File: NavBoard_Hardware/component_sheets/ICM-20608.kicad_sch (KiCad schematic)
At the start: 9 parts

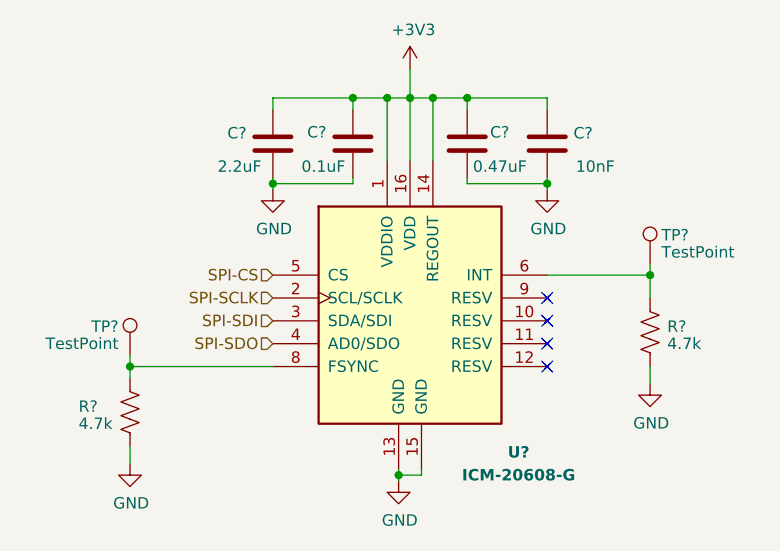
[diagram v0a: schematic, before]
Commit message: Created adapter symbols and footprints
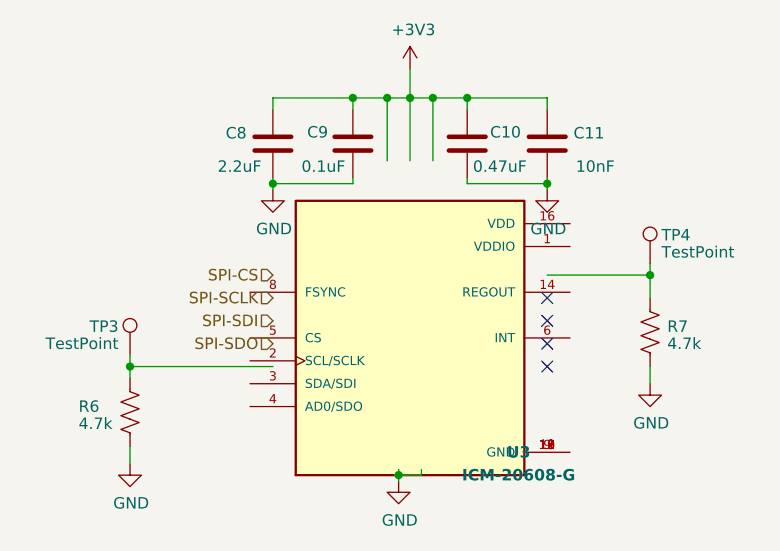
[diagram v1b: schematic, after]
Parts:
- gave numbers to parts that had none: 9
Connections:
- net +3V3: no longer U3.1 (VDDIO), U3.14 (REGOUT), U3.16 (VDD)
- net GND: no longer U3.13 (GND), U3.15 (GND)
- net SPI-CS: no longer U3.5 (CS)
- net SPI-SCLK: no longer U3.2 (SCL/SCLK)
- net SPI-SDI: no longer U3.3 (SDA/SDI)
- net SPI-SDO: no longer U3.4 (AD0/SDO)
- net at R6.1, TP3.1: no longer U3.8 (FSYNC)
- net at R7.1, TP4.1: no longer U3.6 (INT)
- net at U3.10 (GND): now also U3.11 (GND), U3.12 (GND), U3.13 (GND), U3.15 (GND), U3.9 (GND)
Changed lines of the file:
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@@
   (symbol (lib_id "Device:R_US") (at 117.475 106.045 0) (unit 1)
     (in_bom yes) (on_board yes)
-    (property "Reference" "R?" (id 0) (at 111.76 105.41 0)
+    (property "Reference" "R6" (id 0) (at 111.76 105.41 0)
       (effects (font (size 1.27 1.27)) (justify left))
     )
@@
   (symbol (lib_id "Device:R_US") (at 175.26 97.155 0) (unit 1)
     (in_bom yes) (on_board yes)
-    (property "Reference" "R?" (id 0) (at 177.165 96.52 0)
+    (property "Reference" "R7" (id 0) (at 177.165 96.52 0)
       (effects (font (size 1.27 1.27)) (justify left))
     )
@@
   (symbol (lib_id "Device:C") (at 142.24 76.2 0) (unit 1)
     (in_bom yes) (on_board yes)
-    (property "Reference" "C?" (id 0) (at 137.16 74.93 0)
+    (property "Reference" "C9" (id 0) (at 137.16 74.93 0)
       (effects (font (size 1.27 1.27)) (justify left))
     )
@@
   (symbol (lib_id "power:GND") (at 163.83 81.28 0) (unit 1)
     (in_bom yes) (on_board yes)
-    (property "Reference" "#PWR?" (id 0) (at 163.83 87.63 0)
+    (property "Reference" "#PWR014" (id 0) (at 163.83 87.63 0)
       (effects (font (size 1.27 1.27)) hide)
     )
@@
   (symbol (lib_id "Device:C") (at 133.35 76.2 0) (mirror y) (unit 1)
     (in_bom yes) (on_board yes)
-    (property "Reference" "C?" (id 0) (at 130.429 75.0316 0)
+    (property "Reference" "C8" (id 0) (at 130.429 75.0316 0)
       (effects (font (size 1.27 1.27)) (justify left))
     )
@@
   (symbol (lib_id "power:GND") (at 175.26 102.87 0) (unit 1)
     (in_bom yes) (on_board yes)
-    (property "Reference" "#PWR?" (id 0) (at 175.26 109.22 0)
+    (property "Reference" "#PWR015" (id 0) (at 175.26 109.22 0)
       (effects (font (size 1.27 1.27)) hide)
     )
@@
   (symbol (lib_id "Device:C") (at 163.83 76.2 0) (unit 1)
     (in_bom yes) (on_board yes)
-    (property "Reference" "C?" (id 0) (at 166.751 75.0316 0)
+    (property "Reference" "C11" (id 0) (at 166.751 75.0316 0)
       (effects (font (size 1.27 1.27)) (justify left))
     )
@@
   (symbol (lib_id "power:GND") (at 133.35 81.28 0) (unit 1)
     (in_bom yes) (on_board yes)
-    (property "Reference" "#PWR?" (id 0) (at 133.35 87.63 0)
+    (property "Reference" "#PWR011" (id 0) (at 133.35 87.63 0)
       (effects (font (size 1.27 1.27)) hide)
     )
@@
   (symbol (lib_id "power:GND") (at 117.475 111.76 0) (unit 1)
     (in_bom yes) (on_board yes)
-    (property "Reference" "#PWR?" (id 0) (at 117.475 118.11 0)
+    (property "Reference" "#PWR010" (id 0) (at 117.475 118.11 0)
       (effects (font (size 1.27 1.27)) hide)
     )
@@
   (symbol (lib_id "Connector:TestPoint") (at 117.475 99.695 0) (mirror y) (unit 1)
     (in_bom yes) (on_board yes)
-    (property "Reference" "TP?" (id 0) (at 116.205 96.52 0)
+    (property "Reference" "TP3" (id 0) (at 116.205 96.52 0)
       (effects (font (size 1.27 1.27)) (justify left))
     )
@@
   (symbol (lib_id "power:GND") (at 147.32 113.665 0) (unit 1)
     (in_bom yes) (on_board yes)
-    (property "Reference" "#PWR?" (id 0) (at 147.32 120.015 0)
+    (property "Reference" "#PWR012" (id 0) (at 147.32 120.015 0)
       (effects (font (size 1.27 1.27)) hide)
     )
@@
   (symbol (lib_id "Device:C") (at 154.94 76.2 0) (unit 1)
     (in_bom yes) (on_board yes)
-    (property "Reference" "C?" (id 0) (at 157.48 74.93 0)
+    (property "Reference" "C10" (id 0) (at 157.48 74.93 0)
       (effects (font (size 1.27 1.27)) (justify left))
     )
@@
   (symbol (lib_id "MRDT_Sensors:ICM-20608-G") (at 148.59 97.79 0) (unit 1)
     (in_bom yes) (on_board yes)
-    (property "Reference" "U?" (id 0) (at 160.655 110.49 0)
+    (property "Reference" "U3" (id 0) (at 160.655 110.49 0)
       (effects (font (size 1.27 1.27) bold))
     )
@@
   (symbol (lib_id "power:+3V3") (at 148.59 67.945 0) (unit 1)
     (in_bom yes) (on_board yes)
-    (property "Reference" "#PWR?" (id 0) (at 148.59 71.755 0)
+    (property "Reference" "#PWR013" (id 0) (at 148.59 71.755 0)
       (effects (font (size 1.27 1.27)) hide)
     )
@@
   (symbol (lib_id "Connector:TestPoint") (at 175.26 89.535 0) (unit 1)
     (in_bom yes) (on_board yes)
-    (property "Reference" "TP?" (id 0) (at 176.53 86.36 0)
-      (effects (font (size 1.27 1.27)) (justify left))
-    )
+    (property "Reference" "TP4" (id 0) (at 176.53 86.36 0)
+      (effects (font (size 1.27 1.27)) (justify left))
+    )

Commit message: Updated BMI component sheet from Navboard_2023_rev2
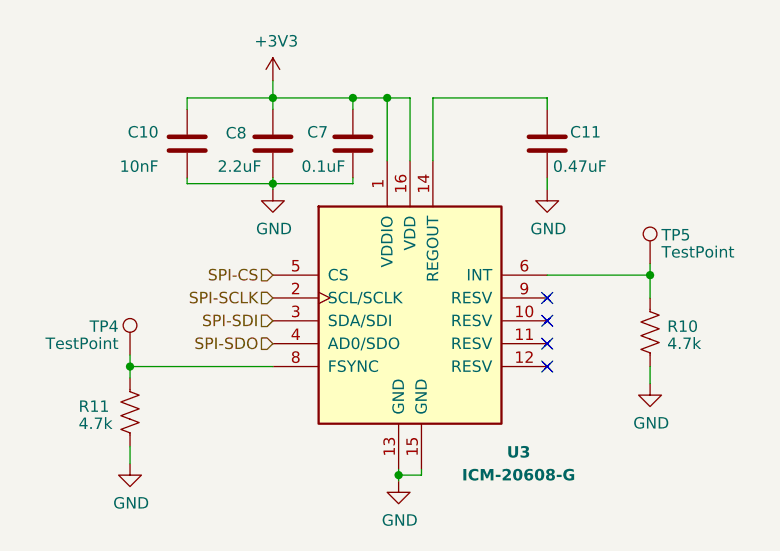
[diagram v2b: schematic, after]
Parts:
- renumbered C11 to C10, C10 to C11, C9 to C7, R7 to R10, R6 to R11, TP3 to TP4, TP4 to TP5
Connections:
- net +3V3: now also U3.1 (VDDIO), U3.16 (VDD); no longer C11.1
- net GND: now also U3.13 (GND), U3.15 (GND)
- net SPI-CS: now also U3.5 (CS)
- net SPI-SCLK: now also U3.2 (SCL/SCLK)
- net SPI-SDI: now also U3.3 (SDA/SDI)
- net SPI-SDO: now also U3.4 (AD0/SDO)
- net at R11.1, TP4.1: now also U3.8 (FSYNC)
- net at R10.1, TP5.1: now also U3.6 (INT)
- net at U3.14 (REGOUT): now also C11.1
- now unconnected: U3.10 (GND), U3.11 (GND), U3.12 (GND), U3.9 (GND)
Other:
- company: Missouri S&T Rover Design Team -> Thomas Francois, Katherine Dunlap, Missouri S&T Mars Rover Design Team
- moved on the sheet: C10, C11

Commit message: Most schematic connections completed
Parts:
- U3: footprint ICM-20608-G:ICM-20608-G -> PQFN50P300X300X80-16N
- renumbered C11 to C10, C10 to C11, C7 to C9, R11 to R6, R10 to R7, TP4 to TP3, TP5 to TP4
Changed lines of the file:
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@@
   (symbol (lib_id "Device:R_US") (at 117.475 106.045 0) (unit 1)
     (in_bom yes) (on_board yes)
-    (property "Reference" "R11" (id 0) (at 111.76 105.41 0)
+    (property "Reference" "R6" (id 0) (at 111.76 105.41 0)
       (effects (font (size 1.27 1.27)) (justify left))
     )
@@
   (symbol (lib_id "Device:R_US") (at 175.26 97.155 0) (unit 1)
     (in_bom yes) (on_board yes)
-    (property "Reference" "R10" (id 0) (at 177.165 96.52 0)
+    (property "Reference" "R7" (id 0) (at 177.165 96.52 0)
       (effects (font (size 1.27 1.27)) (justify left))
     )
@@
   (symbol (lib_id "Device:C") (at 142.24 76.2 0) (unit 1)
     (in_bom yes) (on_board yes)
-    (property "Reference" "C7" (id 0) (at 137.16 74.93 0)
+    (property "Reference" "C9" (id 0) (at 137.16 74.93 0)
       (effects (font (size 1.27 1.27)) (justify left))
     )
@@
   (symbol (lib_id "power:GND") (at 163.83 81.28 0) (unit 1)
     (in_bom yes) (on_board yes)
-    (property "Reference" "#PWR0104" (id 0) (at 163.83 87.63 0)
+    (property "Reference" "#PWR014" (id 0) (at 163.83 87.63 0)
       (effects (font (size 1.27 1.27)) hide)
     )
@@
   (symbol (lib_id "power:GND") (at 175.26 102.87 0) (unit 1)
     (in_bom yes) (on_board yes)
-    (property "Reference" "#PWR0101" (id 0) (at 175.26 109.22 0)
+    (property "Reference" "#PWR015" (id 0) (at 175.26 109.22 0)
       (effects (font (size 1.27 1.27)) hide)
     )
@@
   (symbol (lib_id "Device:C") (at 123.825 76.2 0) (mirror y) (unit 1)
     (in_bom yes) (on_board yes)
-    (property "Reference" "C10" (id 0) (at 120.65 74.93 0)
+    (property "Reference" "C11" (id 0) (at 120.65 74.93 0)
       (effects (font (size 1.27 1.27)) (justify left))
     )
@@
   (symbol (lib_id "power:GND") (at 133.35 81.28 0) (unit 1)
     (in_bom yes) (on_board yes)
-    (property "Reference" "#PWR0106" (id 0) (at 133.35 87.63 0)
+    (property "Reference" "#PWR011" (id 0) (at 133.35 87.63 0)
       (effects (font (size 1.27 1.27)) hide)
     )
@@
   (symbol (lib_id "power:GND") (at 117.475 111.76 0) (unit 1)
     (in_bom yes) (on_board yes)
-    (property "Reference" "#PWR0107" (id 0) (at 117.475 118.11 0)
+    (property "Reference" "#PWR010" (id 0) (at 117.475 118.11 0)
       (effects (font (size 1.27 1.27)) hide)
     )
@@
   (symbol (lib_id "Connector:TestPoint") (at 117.475 99.695 0) (mirror y) (unit 1)
     (in_bom yes) (on_board yes)
-    (property "Reference" "TP4" (id 0) (at 116.205 96.52 0)
+    (property "Reference" "TP3" (id 0) (at 116.205 96.52 0)
       (effects (font (size 1.27 1.27)) (justify left))
     )
@@
   (symbol (lib_id "power:GND") (at 147.32 113.665 0) (unit 1)
     (in_bom yes) (on_board yes)
-    (property "Reference" "#PWR0105" (id 0) (at 147.32 120.015 0)
+    (property "Reference" "#PWR012" (id 0) (at 147.32 120.015 0)
       (effects (font (size 1.27 1.27)) hide)
     )
@@
   (symbol (lib_id "Device:C") (at 163.83 76.2 0) (unit 1)
     (in_bom yes) (on_board yes)
-    (property "Reference" "C11" (id 0) (at 166.37 74.93 0)
+    (property "Reference" "C10" (id 0) (at 166.37 74.93 0)
       (effects (font (size 1.27 1.27)) (justify left))
     )
@@
       (effects (font (size 1.27 1.27) bold))
     )
-    (property "Footprint" "ICM-20608-G:ICM-20608-G" (id 2) (at 173.99 85.725 0)
+    (property "Footprint" "PQFN50P300X300X80-16N" (id 2) (at 173.99 85.725 0)
       (effects (font (size 1.27 1.27)) (justify left bottom) hide)
     )
@@
   (symbol (lib_id "power:+3V3") (at 133.35 69.215 0) (unit 1)
     (in_bom yes) (on_board yes)
-    (property "Reference" "#PWR0103" (id 0) (at 133.35 73.025 0)
+    (property "Reference" "#PWR013" (id 0) (at 133.35 73.025 0)
       (effects (font (size 1.27 1.27)) hide)
     )
@@
   (symbol (lib_id "Connector:TestPoint") (at 175.26 89.535 0) (unit 1)
     (in_bom yes) (on_board yes)
-    (property "Reference" "TP5" (id 0) (at 176.53 86.36 0)
-      (effects (font (size 1.27 1.27)) (justify left))
-    )
+    (property "Reference" "TP4" (id 0) (at 176.53 86.36 0)
+      (effects (font (size 1.27 1.27)) (justify left))
+    )

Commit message: Annotated Schematic, assigned footprints, recovered accelerometer footprints
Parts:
- U3: footprint PQFN50P300X300X80-16N -> Nav_Board:ICM-20608-G
- renumbered C9 to C10, C10 to C11, C11 to C8, C8 to C9, R7 to R6, R6 to R7, TP4 to TP3, TP3 to TP4
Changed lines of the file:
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@@
   (symbol (lib_id "Device:R_US") (at 117.475 106.045 0) (unit 1)
     (in_bom yes) (on_board yes)
-    (property "Reference" "R6" (id 0) (at 111.76 105.41 0)
+    (property "Reference" "R7" (id 0) (at 111.76 105.41 0)
       (effects (font (size 1.27 1.27)) (justify left))
     )
@@
   (symbol (lib_id "Device:R_US") (at 175.26 97.155 0) (unit 1)
     (in_bom yes) (on_board yes)
-    (property "Reference" "R7" (id 0) (at 177.165 96.52 0)
+    (property "Reference" "R6" (id 0) (at 177.165 96.52 0)
       (effects (font (size 1.27 1.27)) (justify left))
     )
@@
   (symbol (lib_id "Device:C") (at 142.24 76.2 0) (unit 1)
     (in_bom yes) (on_board yes)
-    (property "Reference" "C9" (id 0) (at 137.16 74.93 0)
+    (property "Reference" "C10" (id 0) (at 137.16 74.93 0)
       (effects (font (size 1.27 1.27)) (justify left))
     )
@@
   (symbol (lib_id "power:GND") (at 163.83 81.28 0) (unit 1)
     (in_bom yes) (on_board yes)
-    (property "Reference" "#PWR014" (id 0) (at 163.83 87.63 0)
+    (property "Reference" "#PWR015" (id 0) (at 163.83 87.63 0)
       (effects (font (size 1.27 1.27)) hide)
     )
@@
   (symbol (lib_id "Device:C") (at 133.35 76.2 0) (mirror y) (unit 1)
     (in_bom yes) (on_board yes)
-    (property "Reference" "C8" (id 0) (at 130.429 75.0316 0)
+    (property "Reference" "C9" (id 0) (at 130.429 75.0316 0)
       (effects (font (size 1.27 1.27)) (justify left))
     )
@@
   (symbol (lib_id "power:GND") (at 175.26 102.87 0) (unit 1)
     (in_bom yes) (on_board yes)
-    (property "Reference" "#PWR015" (id 0) (at 175.26 109.22 0)
+    (property "Reference" "#PWR016" (id 0) (at 175.26 109.22 0)
       (effects (font (size 1.27 1.27)) hide)
     )
@@
   (symbol (lib_id "Device:C") (at 123.825 76.2 0) (mirror y) (unit 1)
     (in_bom yes) (on_board yes)
-    (property "Reference" "C11" (id 0) (at 120.65 74.93 0)
+    (property "Reference" "C8" (id 0) (at 120.65 74.93 0)
       (effects (font (size 1.27 1.27)) (justify left))
     )
@@
   (symbol (lib_id "power:GND") (at 133.35 81.28 0) (unit 1)
     (in_bom yes) (on_board yes)
-    (property "Reference" "#PWR011" (id 0) (at 133.35 87.63 0)
+    (property "Reference" "#PWR014" (id 0) (at 133.35 87.63 0)
       (effects (font (size 1.27 1.27)) hide)
     )
@@
   (symbol (lib_id "power:GND") (at 117.475 111.76 0) (unit 1)
     (in_bom yes) (on_board yes)
-    (property "Reference" "#PWR010" (id 0) (at 117.475 118.11 0)
+    (property "Reference" "#PWR017" (id 0) (at 117.475 118.11 0)
       (effects (font (size 1.27 1.27)) hide)
     )
@@
   (symbol (lib_id "Connector:TestPoint") (at 117.475 99.695 0) (mirror y) (unit 1)
     (in_bom yes) (on_board yes)
-    (property "Reference" "TP3" (id 0) (at 116.205 96.52 0)
+    (property "Reference" "TP4" (id 0) (at 116.205 96.52 0)
       (effects (font (size 1.27 1.27)) (justify left))
     )
@@
   (symbol (lib_id "power:GND") (at 147.32 113.665 0) (unit 1)
     (in_bom yes) (on_board yes)
-    (property "Reference" "#PWR012" (id 0) (at 147.32 120.015 0)
+    (property "Reference" "#PWR018" (id 0) (at 147.32 120.015 0)
       (effects (font (size 1.27 1.27)) hide)
     )
@@
   (symbol (lib_id "Device:C") (at 163.83 76.2 0) (unit 1)
     (in_bom yes) (on_board yes)
-    (property "Reference" "C10" (id 0) (at 166.37 74.93 0)
+    (property "Reference" "C11" (id 0) (at 166.37 74.93 0)
       (effects (font (size 1.27 1.27)) (justify left))
     )
@@
       (effects (font (size 1.27 1.27) bold))
     )
-    (property "Footprint" "PQFN50P300X300X80-16N" (id 2) (at 173.99 85.725 0)
+    (property "Footprint" "Nav_Board:ICM-20608-G" (id 2) (at 173.99 85.725 0)
       (effects (font (size 1.27 1.27)) (justify left bottom) hide)
     )
@@
   (symbol (lib_id "Connector:TestPoint") (at 175.26 89.535 0) (unit 1)
     (in_bom yes) (on_board yes)
-    (property "Reference" "TP4" (id 0) (at 176.53 86.36 0)
-      (effects (font (size 1.27 1.27)) (justify left))
-    )
+    (property "Reference" "TP3" (id 0) (at 176.53 86.36 0)
+      (effects (font (size 1.27 1.27)) (justify left))
+    )

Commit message: Completed routing, added 3D models to IMUs
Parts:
- TP3, TP4: footprint TestPoint:TestPoint_Pad_D2.0mm -> TestPoint:TestPoint_Pad_D1.5mm
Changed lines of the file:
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@@
       (effects (font (size 1.27 1.27)) (justify left))
     )
-    (property "Footprint" "TestPoint:TestPoint_Pad_D2.0mm" (id 2) (at 112.395 99.695 0)
+    (property "Footprint" "TestPoint:TestPoint_Pad_D1.5mm" (id 2) (at 112.395 99.695 0)
       (effects (font (size 1.27 1.27)) hide)
     )
@@
       (effects (font (size 1.27 1.27)) (justify left))
     )
-    (property "Footprint" "TestPoint:TestPoint_Pad_D2.0mm" (id 2) (at 180.34 89.535 0)
+    (property "Footprint" "TestPoint:TestPoint_Pad_D1.5mm" (id 2) (at 180.34 89.535 0)
       (effects (font (size 1.27 1.27)) hide)
     )

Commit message: Annotated schematic pages
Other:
- company: Thomas Francois, Katherine Dunlap, Missouri S&T Mars Rover Design Team -> Thomas Francois, Missouri S&T Mars Rover Design Team
- title: ICM-20608-G Inertial Measurement Unit -> MRDT NavBoard - ICM-20608-G
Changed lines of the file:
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@@
   (paper "A4")
   (title_block
-    (title "ICM-20608-G Inertial Measurement Unit")
+    (title "MRDT NavBoard - ICM-20608-G")
     (date "2022-09-15")
-    (rev "2, 2023")
-    (company "Thomas Francois, Katherine Dunlap, Missouri S&T Mars Rover Design Team")
-    (comment 1 "ICM-2060B-G IMU & Supporting Components")
+    (rev "1, 2023")
+    (company "Thomas Francois, Missouri S&T Mars Rover Design Team")
+    (comment 1 "Inertial Measurement Unit and Supporting Components")
     (comment 2 "Provides Position & Acceleration Data")
   )

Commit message: Realized this could all fit on a single board
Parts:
- renumbered U3 to U4
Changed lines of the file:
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@@
   (symbol (lib_id "power:GND") (at 163.83 81.28 0) (unit 1)
     (in_bom yes) (on_board yes)
-    (property "Reference" "#PWR015" (id 0) (at 163.83 87.63 0)
+    (property "Reference" "#PWR026" (id 0) (at 163.83 87.63 0)
       (effects (font (size 1.27 1.27)) hide)
     )
@@
   (symbol (lib_id "power:GND") (at 175.26 102.87 0) (unit 1)
     (in_bom yes) (on_board yes)
-    (property "Reference" "#PWR016" (id 0) (at 175.26 109.22 0)
+    (property "Reference" "#PWR027" (id 0) (at 175.26 109.22 0)
       (effects (font (size 1.27 1.27)) hide)
     )
@@
   (symbol (lib_id "power:GND") (at 133.35 81.28 0) (unit 1)
     (in_bom yes) (on_board yes)
-    (property "Reference" "#PWR014" (id 0) (at 133.35 87.63 0)
+    (property "Reference" "#PWR025" (id 0) (at 133.35 87.63 0)
       (effects (font (size 1.27 1.27)) hide)
     )
@@
   (symbol (lib_id "power:GND") (at 117.475 111.76 0) (unit 1)
     (in_bom yes) (on_board yes)
-    (property "Reference" "#PWR017" (id 0) (at 117.475 118.11 0)
+    (property "Reference" "#PWR028" (id 0) (at 117.475 118.11 0)
       (effects (font (size 1.27 1.27)) hide)
     )
@@
   (symbol (lib_id "power:GND") (at 147.32 113.665 0) (unit 1)
     (in_bom yes) (on_board yes)
-    (property "Reference" "#PWR018" (id 0) (at 147.32 120.015 0)
+    (property "Reference" "#PWR029" (id 0) (at 147.32 120.015 0)
       (effects (font (size 1.27 1.27)) hide)
     )
@@
   (symbol (lib_id "MRDT_Sensors:ICM-20608-G") (at 148.59 97.79 0) (unit 1)
     (in_bom yes) (on_board yes)
-    (property "Reference" "U3" (id 0) (at 160.655 110.49 0)
+    (property "Reference" "U4" (id 0) (at 160.655 110.49 0)
       (effects (font (size 1.27 1.27) bold))
     )
@@
   (symbol (lib_id "power:+3V3") (at 133.35 69.215 0) (unit 1)
     (in_bom yes) (on_board yes)
-    (property "Reference" "#PWR013" (id 0) (at 133.35 73.025 0)
+    (property "Reference" "#PWR024" (id 0) (at 133.35 73.025 0)
       (effects (font (size 1.27 1.27)) hide)
     )
